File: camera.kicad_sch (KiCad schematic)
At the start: 1 part, among them J10 Conn_01x24_MountingPin

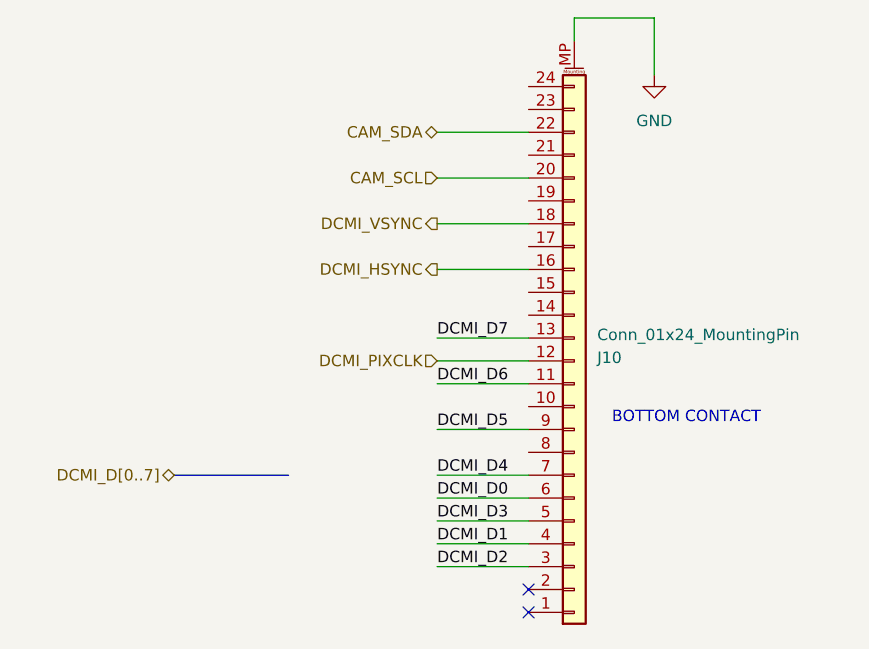
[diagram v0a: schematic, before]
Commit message: Removing Camera, create alternative footprint for SPI LCD conn
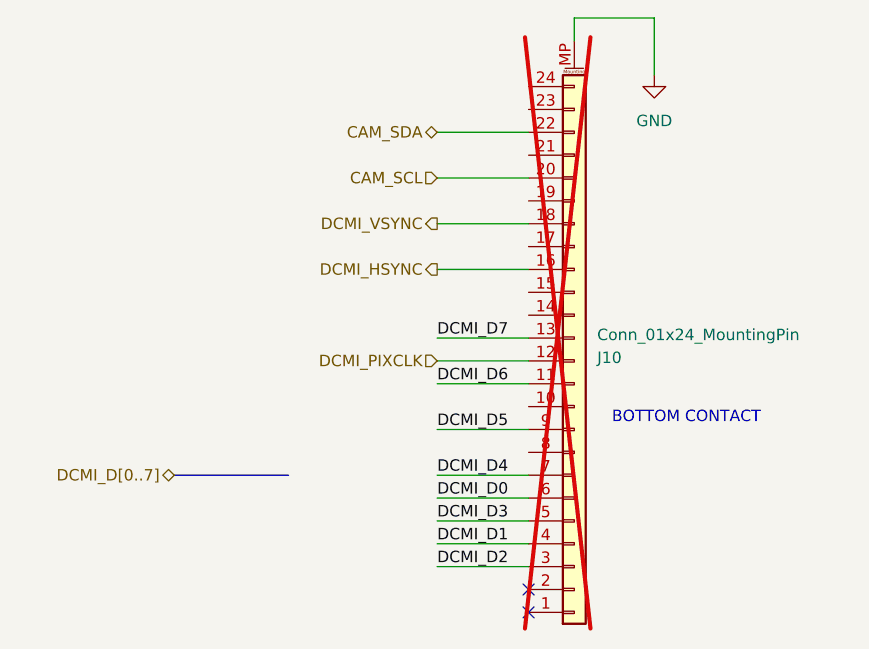
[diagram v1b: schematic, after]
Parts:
- J10: now not fitted; now left out of the parts list
